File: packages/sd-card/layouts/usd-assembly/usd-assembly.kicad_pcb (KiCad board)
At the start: 2 copper layers, 5 parts

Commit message: bigg
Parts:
- moved R1 1.16 mm to (66.6, 53.0)
- moved R2 1.13 mm to (65.4, 53.0)
- moved Card1 0.48 mm to (70.8, 60.8)
- moved R3 0.10 mm to (68.7, 53.0)
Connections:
- net DAT2 renamed pins[8]
- net line-0 renamed pins[0]
- net line-1 renamed pins[6]
- net line-2 renamed pins[7]

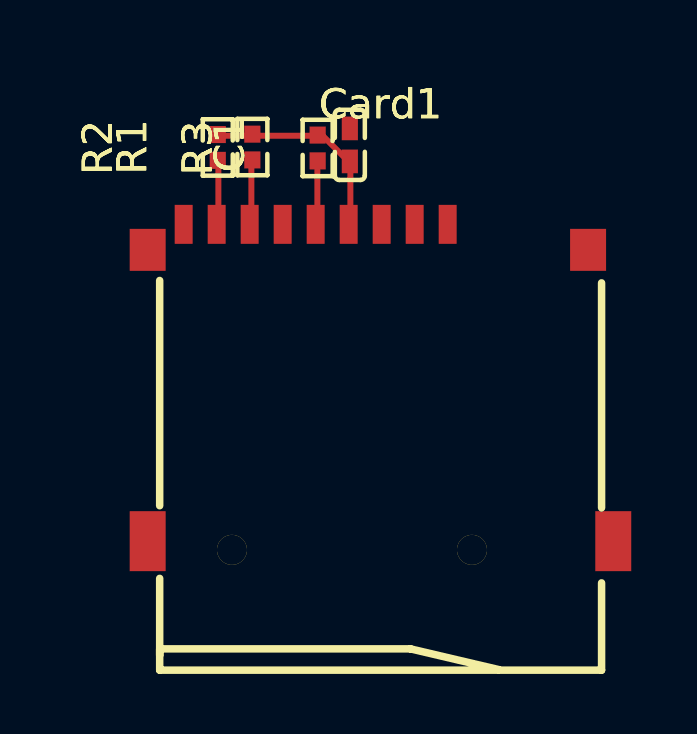
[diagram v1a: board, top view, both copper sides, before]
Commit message: port example over to usage
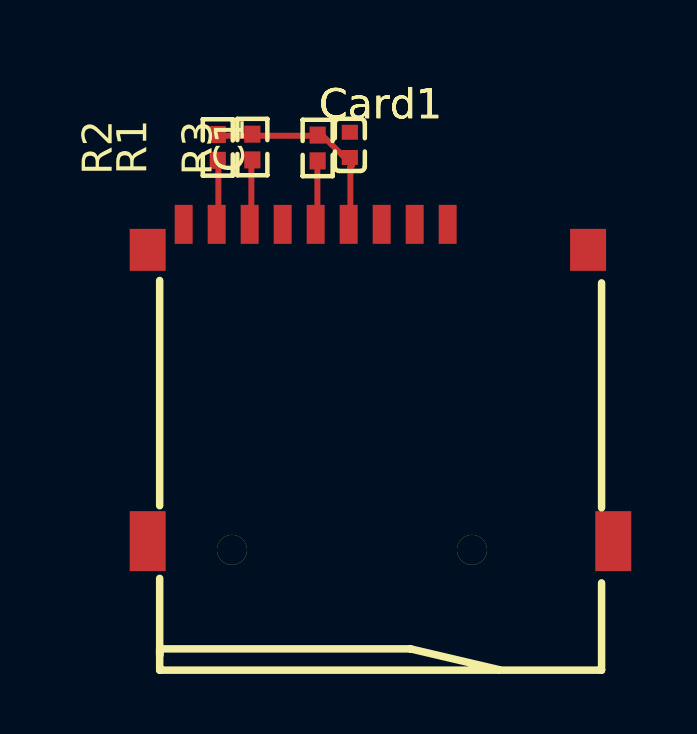
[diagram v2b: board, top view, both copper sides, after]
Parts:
- C1: value 100nF ±10% 16V X7R -> 100nF
- R1, R2, R3: value 10kΩ ±1% 62.5mW -> 10kΩ
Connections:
- net CLK renamed SCLK
- net gnd renamed lv
- net pins[6] renamed MISO
- net pins[7] renamed MOSI
- Card1 pad : net -> (no net)
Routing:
- net hv: track 6.71 -> 0.00 mm
- net 4: track 0.00 -> 6.71 mm
